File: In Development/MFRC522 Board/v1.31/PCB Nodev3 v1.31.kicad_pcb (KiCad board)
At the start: 2 copper layers, 120 x 50 mm, 45 parts, among them P1 ESP32 NODEMCU DEVKIT1 LEFT HE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, P2 ESP32 NODEMCU DEVKIT1 RIGHT H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, Q2 Q_NPN_BEC, U1 MFRC522, Y1 27.12 MHz

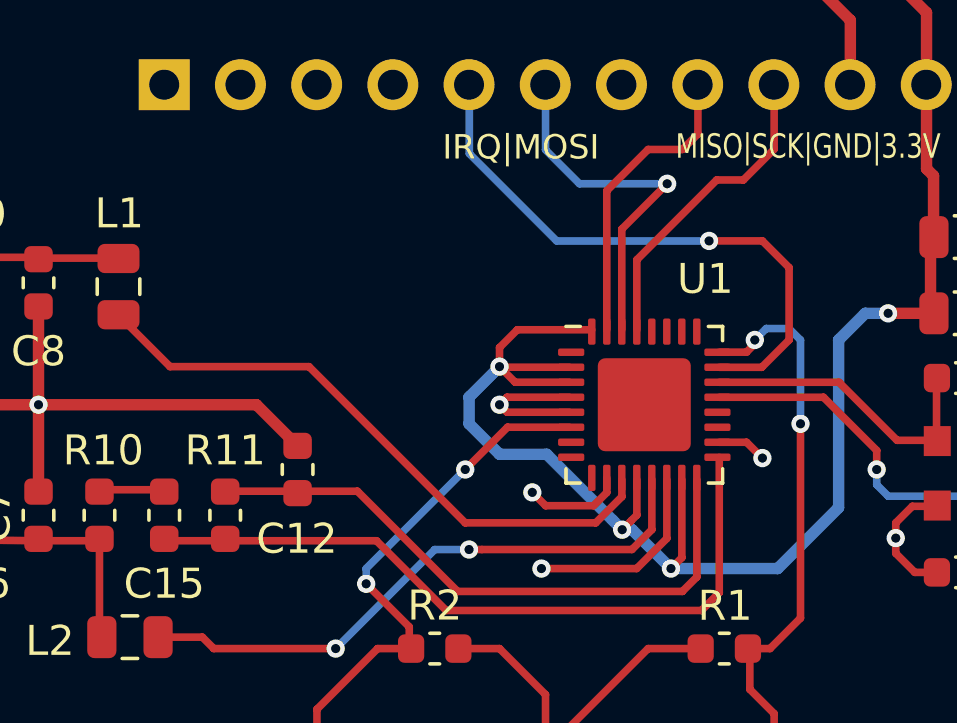
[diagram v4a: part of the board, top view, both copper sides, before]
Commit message: added thermal pads
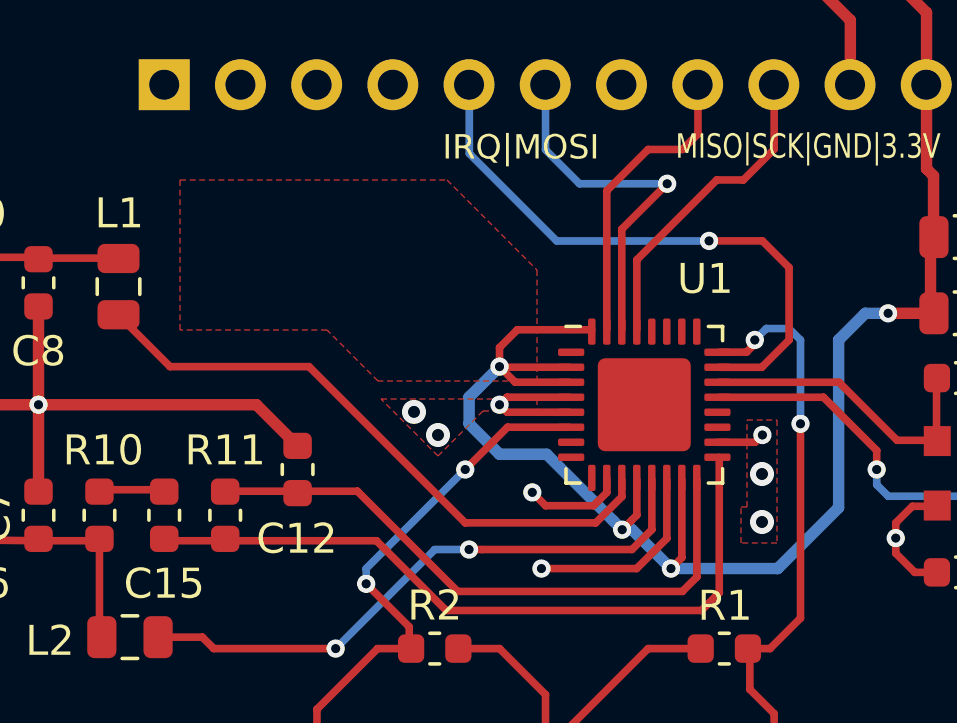
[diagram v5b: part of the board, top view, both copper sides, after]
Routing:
- net GND: vias 19 -> 23
- added copper zone on F.Cu, net +3V3
- added copper zone on F.Cu, net GND
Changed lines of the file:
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@@
     (thickness 1.6)
     (drawings 434)
-    (tracks 342)
+    (tracks 346)
     (zones 0)
     (modules 45)
@@
   (segment (start 127.508 81.915) (end 127.757 82.164) (width 0.254) (layer F.Cu) (net 1))
   (segment (start 127.757 82.164) (end 129.834 82.164) (width 0.254) (layer F.Cu) (net 1))
-  (segment (start 134.834 83.166) (end 135.744 83.166) (width 0.254) (layer F.Cu) (net 1))
-  (segment (start 135.744 83.166) (end 136.271 83.693) (width 0.254) (layer F.Cu) (net 1))
   (segment (start 143.875 76.327) (end 143.875 77.581) (width 0.381) (layer F.Cu) (net 1))
   (segment (start 143.875 77.581) (end 143.891 77.597) (width 0.381) (layer F.Cu) (net 1))
@@
   (via (at 128.839 97.983) (size 0.61) (drill 0.305) (layers F.Cu B.Cu) (net 1))
   (via (at 127.508 81.915) (size 0.61) (drill 0.305) (layers F.Cu B.Cu) (net 1))
-  (via (at 136.271 83.693) (size 0.61) (drill 0.305) (layers F.Cu B.Cu) (net 1))
+  (via (at 136.271 82.923635) (size 0.61) (drill 0.305) (layers F.Cu B.Cu) (net 1))
   (via (at 143.891 77.597) (size 0.61) (drill 0.305) (layers F.Cu B.Cu) (net 1))
   (via (at 140.716 86.36) (size 0.61) (drill 0.305) (layers F.Cu B.Cu) (net 1))
@@
   (segment (start 131.084 84.840852) (end 131.084 84.3525) (width 0.254) (layer F.Cu) (net 1))
   (segment (start 128.6002 84.836) (end 129.0447 85.2805) (width 0.254) (layer F.Cu) (net 1))
+  (segment (start 136.029635 83.165) (end 136.271 82.923635) (width 0.254) (layer F.Cu) (net 1))
+  (segment (start 134.7715 83.165) (end 136.029635 83.165) (width 0.254) (layer F.Cu) (net 1))
+  (via (at 136.25736 84.223635) (size 0.8) (drill 0.4) (layers F.Cu B.Cu) (net 1))
+  (via (at 136.25736 85.823635) (size 0.8) (drill 0.4) (layers F.Cu B.Cu) (net 1))
+  (via (at 124.65736 82.153635) (size 0.8) (drill 0.4) (layers F.Cu B.Cu) (net 1))
+  (via (at 125.45736 82.923635) (size 0.8) (drill 0.4) (layers F.Cu B.Cu) (net 1))
   (segment (start 138.303 101.727) (end 136.906 103.124) (width 0.508) (layer F.Cu) (net 2))
   (segment (start 136.906 103.124) (end 135.088 103.124) (width 0.508) (layer F.Cu) (net 2))
@@
       )
     )
+  )
+  (zone (net 5) (net_name +3V3) (layer F.Cu) (hatch edge 0.508)
+    (connect_pads (clearance 0.508))
+    (min_thickness 0.254)
+    (fill yes (arc_segments 32) (thermal_gap 0.508) (thermal_bridge_width 0.508))
+    (polygon
+      (pts
+        (xy 128.75736 77.423635) (xy 128.75736 81.123635) (xy 123.45736 81.123635) (xy 121.75736 79.423635) (xy 116.85736 79.423635)
+        (xy 116.85736 74.423635) (xy 125.75736 74.423635)
+      )
+    )
+  )
+  (zone (net 1) (net_name GND) (layer F.Cu) (hatch edge 0.508)
+    (connect_pads (clearance 0.508))
+    (min_thickness 0.254)
+    (fill yes (arc_segments 32) (thermal_gap 0.508) (thermal_bridge_width 0.508))
+    (polygon
+      (pts
+        (xy 136.75736 86.523635) (xy 135.55736 86.523635) (xy 135.55736 85.323635) (xy 135.75736 85.323635) (xy 135.75736 82.423635)
+        (xy 136.75736 82.423635)
+      )
+    )
+  )
+  (zone (net 1) (net_name GND) (layer F.Cu) (hatch edge 0.508)
+    (connect_pads (clearance 0.508))
+    (min_thickness 0.254)
+    (fill yes (arc_segments 32) (thermal_gap 0.508) (thermal_bridge_width 0.508))
+    (polygon
+      (pts
+        (xy 128.75736 82.123635) (xy 126.95736 82.123635) (xy 125.45736 83.623635) (xy 123.55736 81.723635) (xy 128.75736 81.723635)
+      )
+    )

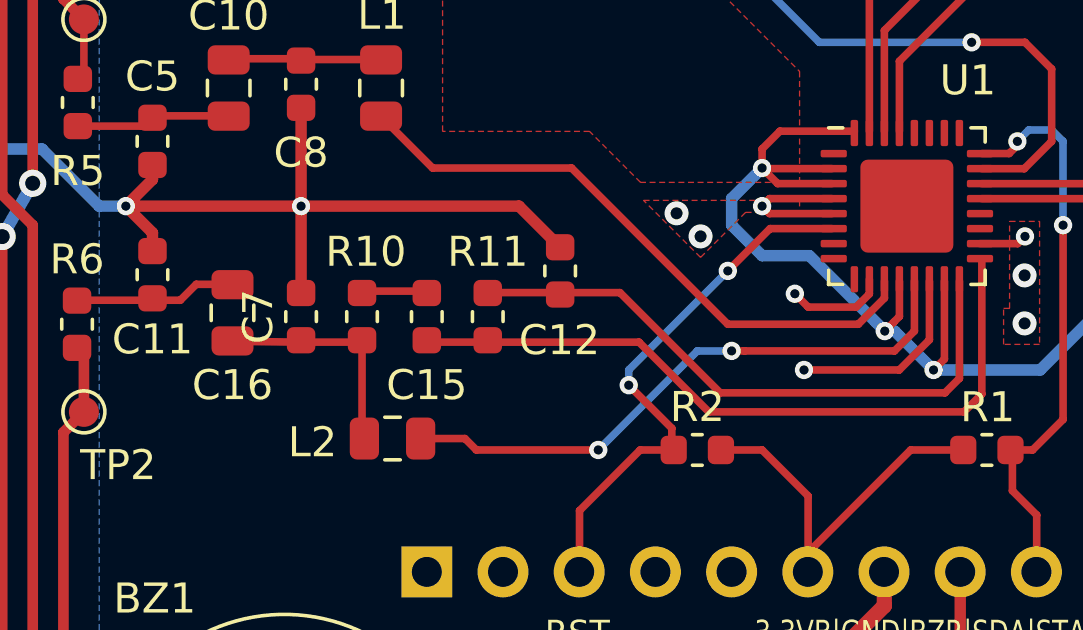
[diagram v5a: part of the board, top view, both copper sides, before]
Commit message: MFRC522 silkscreen edit, LED thermal improvement
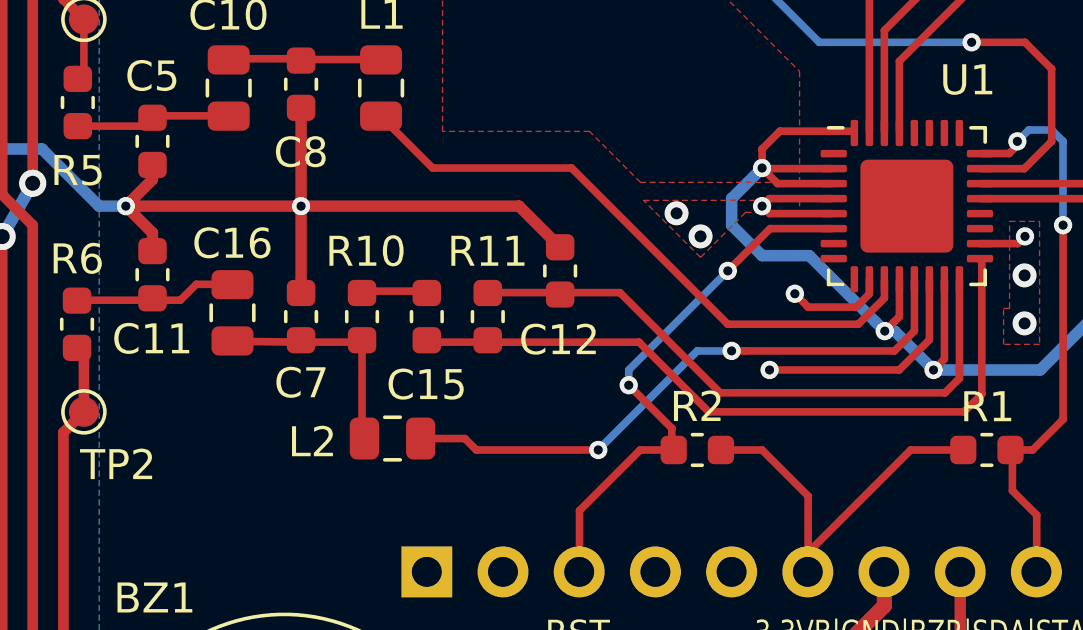
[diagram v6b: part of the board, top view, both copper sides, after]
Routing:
- net GND: track 851.8 -> 852.9 mm
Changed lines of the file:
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@@
     (tags capacitor)
     (attr smd)
-    (fp_text reference C16 (at 2.413 0 180) (layer F.SilkS)
+    (fp_text reference C16 (at -2.297365 -0.00236 180) (layer F.SilkS)
       (effects (font (size 1 1) (thickness 0.15)))
     )
@@
     (tags capacitor)
     (attr smd)
-    (fp_text reference C7 (at 0 -1.43 90) (layer F.SilkS)
+    (fp_text reference C7 (at -2.225635 0.01636 180) (layer F.SilkS)
       (effects (font (size 1 1) (thickness 0.15)))
     )
@@
   (segment (start 106.299 81.915) (end 107.188 81.026) (width 0.381) (layer F.Cu) (net 1))
   (segment (start 107.188 81.026) (end 107.188 80.606) (width 0.381) (layer F.Cu) (net 1))
-  (segment (start 133.086 84.415) (end 133.086 86.37) (width 0.254) (layer F.Cu) (net 1))
-  (segment (start 133.086 86.37) (end 132.08 87.376) (width 0.254) (layer F.Cu) (net 1))
-  (segment (start 132.08 87.376) (end 128.905 87.376) (width 0.254) (layer F.Cu) (net 1))
   (segment (start 46.299 83.566) (end 46.299 103.886) (width 0.356) (layer F.Cu) (net 1))
   (segment (start 46.299 103.886) (end 47.823 105.41) (width 0.356) (layer F.Cu) (net 1))
@@
   (via (at 112.141 81.915) (size 0.61) (drill 0.305) (layers F.Cu B.Cu) (net 1))
   (via (at 106.299 81.915) (size 0.61) (drill 0.305) (layers F.Cu B.Cu) (net 1))
-  (via (at 128.905 87.376) (size 0.61) (drill 0.305) (layers F.Cu B.Cu) (net 1))
+  (via (at 127.75736 87.376) (size 0.61) (drill 0.305) (layers F.Cu B.Cu) (net 1))
   (via (at 46.299 83.566) (size 0.907) (drill 0.5) (layers F.Cu B.Cu) (net 1))
   (via (at 47.315 81.534) (size 0.907) (drill 0.5) (layers F.Cu B.Cu) (net 1))
@@
   (via (at 124.65736 82.153635) (size 0.8) (drill 0.4) (layers F.Cu B.Cu) (net 1))
   (via (at 125.45736 82.923635) (size 0.8) (drill 0.4) (layers F.Cu B.Cu) (net 1))
+  (segment (start 132.08 87.376) (end 127.75736 87.376) (width 0.254) (layer F.Cu) (net 1))
+  (segment (start 133.086 84.415) (end 133.086 86.37) (width 0.254) (layer F.Cu) (net 1))
+  (segment (start 133.086 86.37) (end 132.08 87.376) (width 0.254) (layer F.Cu) (net 1))
   (segment (start 138.303 101.727) (end 136.906 103.124) (width 0.508) (layer F.Cu) (net 2))
   (segment (start 136.906 103.124) (end 135.088 103.124) (width 0.508) (layer F.Cu) (net 2))
